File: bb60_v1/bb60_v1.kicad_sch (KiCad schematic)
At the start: 0 parts

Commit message: added microcontroller, decoupling capacitors
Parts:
- added C1, C2, C3, C4, C5: 100nF, symbol Device:C_Small
- added C6: 10uF, symbol Device:C_Small
- added U1: STM32F072CBTx, Package_QFP:LQFP-48_7x7mm_P0.5mm, symbol MCU_ST_STM32F0:STM32F072CBTx
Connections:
- new net +3.3V: C1.1, C2.1, C3.1, C4.1, C5.1, C6.1, U1.1 (VBAT), U1.24 (VDD), U1.36 (VDDIO2), U1.48 (VDD), U1.9 (VDDA)
- new net GND: C1.2, C2.2, C3.2, C4.2, C5.2, C6.2, U1.23 (VSS), U1.35 (VSS), U1.47 (VSS), U1.8 (VSSA)

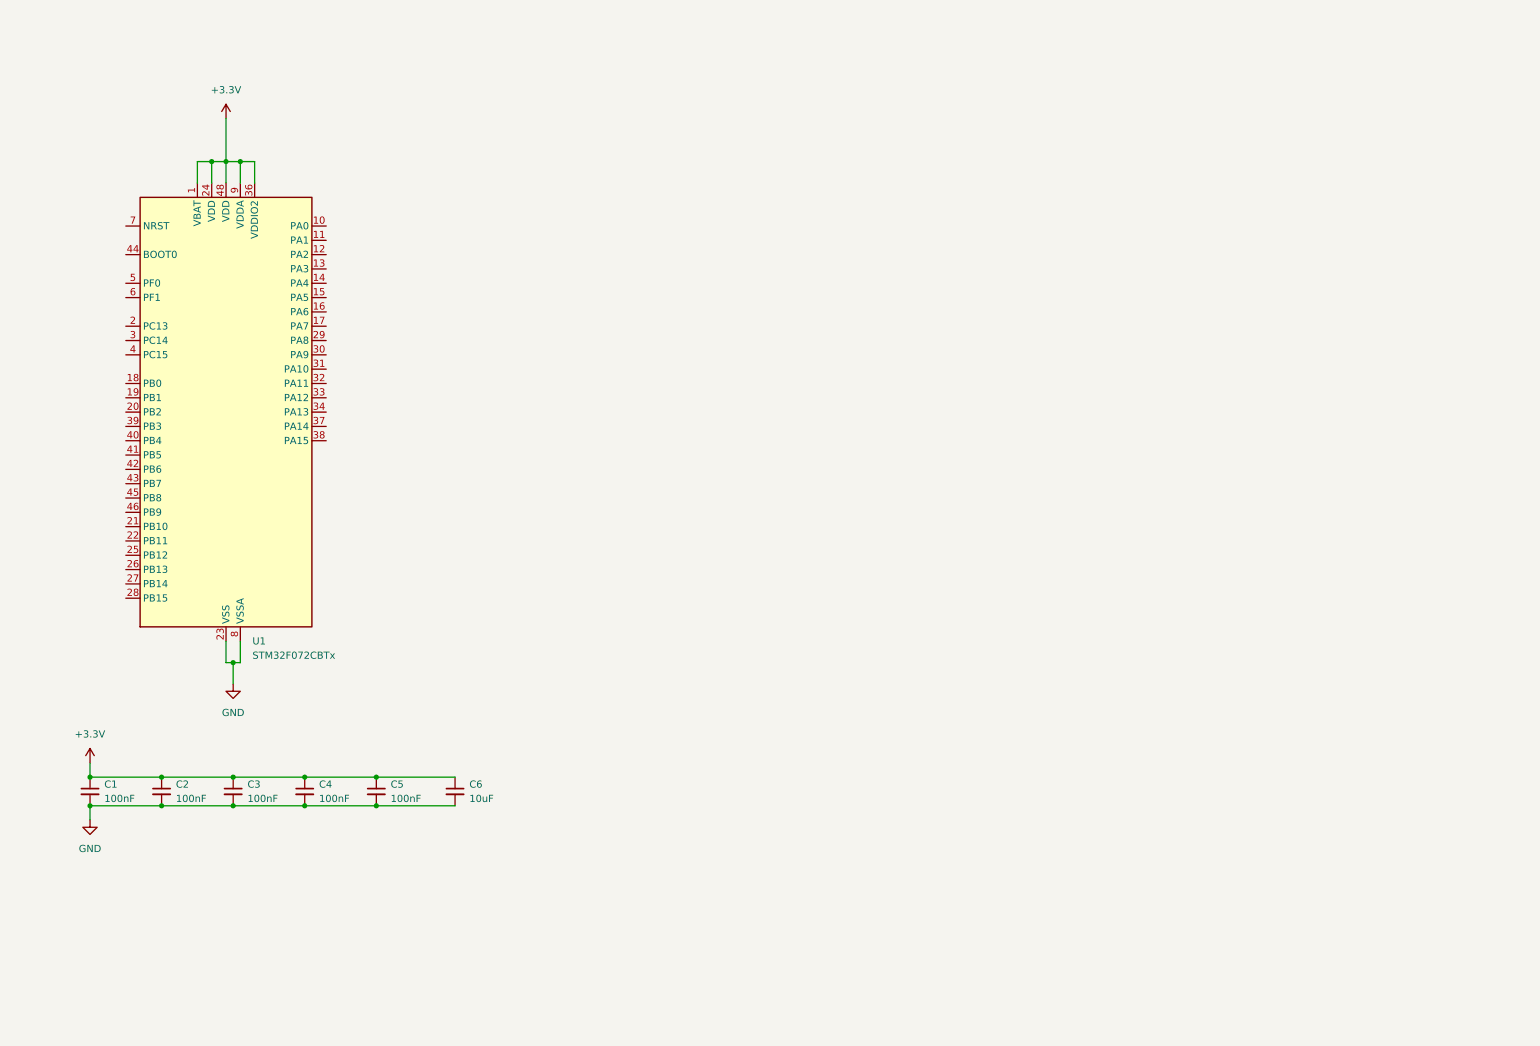
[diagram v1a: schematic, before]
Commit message: added voltage regulator, jst connector, matrix
voltage regular and matrix are unfinished
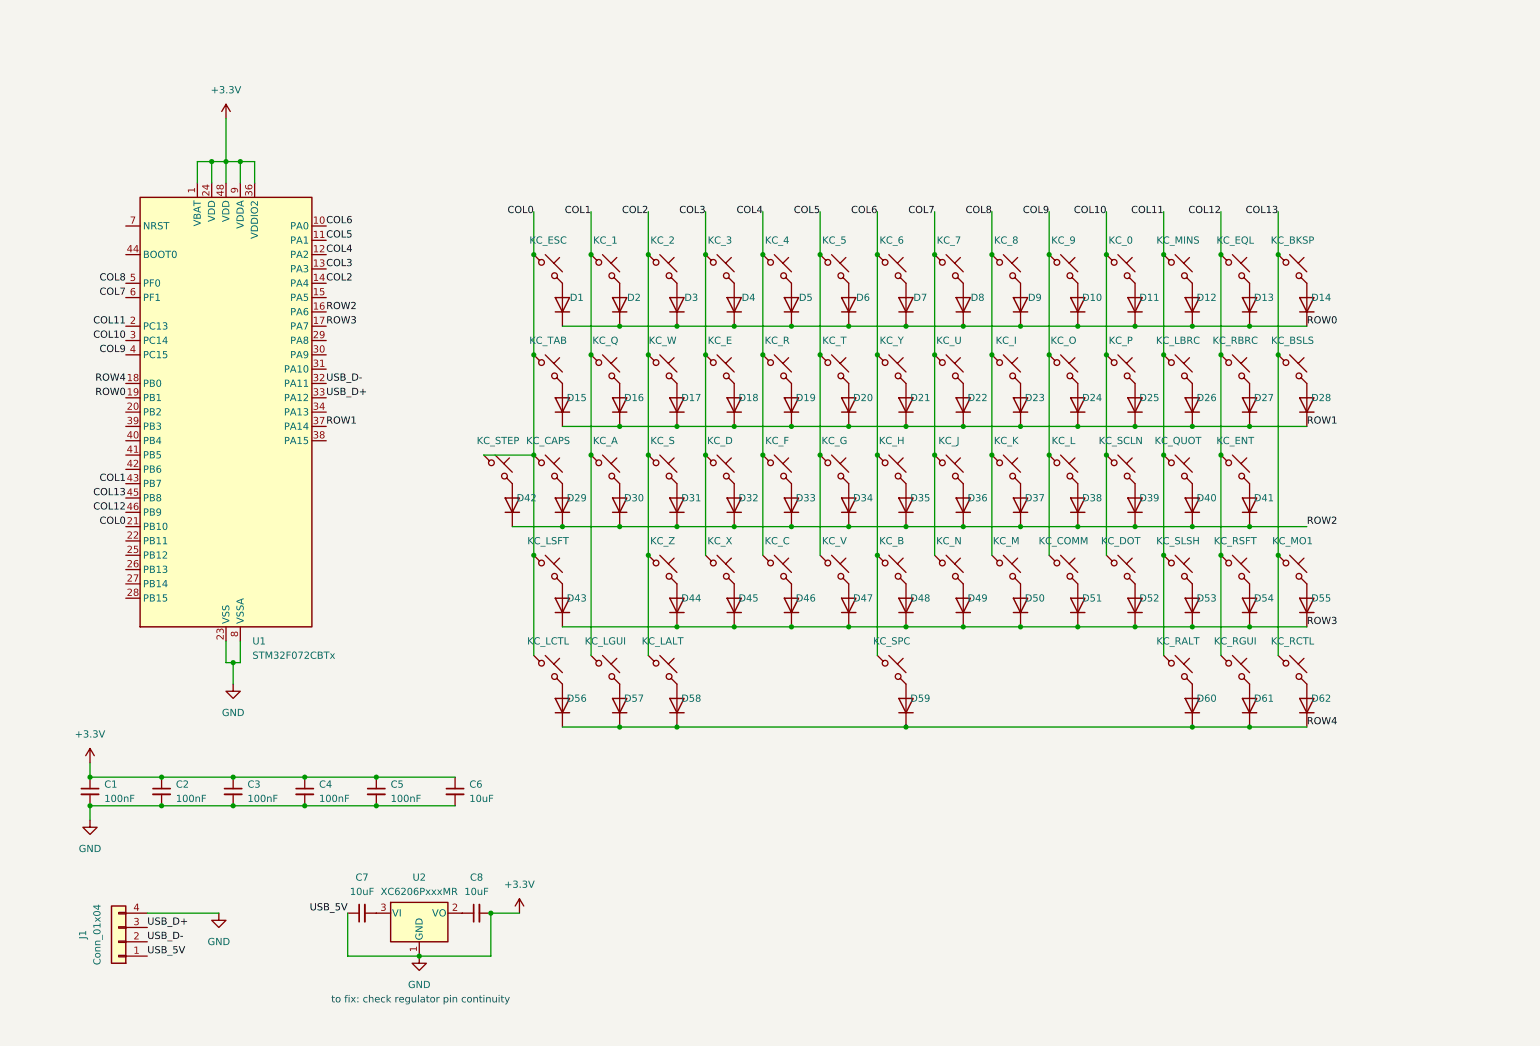
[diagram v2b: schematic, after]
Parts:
- added C7, C8: 10uF, symbol Device:C_Small
- added D1, D10, D11, D12, D13, D14, D15, D16, D17, D18, D19, D2, D20, D21, D22, D23, D24, D25, D26, D27, D28, D29, D3, D30, D31, D32, D33, D34, D35, D36, D37, D38, D39, D4, D40, D41, D42, D43, D44, D45, D46, D47, D48, D49, D5, D50, D51, D52, D53, D54, D55, D56, D57, D58, D59, D6, D60, D61, D62, D7, D8, D9: 1N4148, Diode_THT:D_DO-35_SOD27_P7.62mm_Horizontal, symbol Diode:1N4148
- added J1: Conn_01x04, Connector_JST:JST_SH_SM04B-SRSS-TB_1x04-1MP_P1.00mm_Horizontal, symbol Connector_Generic:Conn_01x04
- added KC_0, KC_1, KC_2, KC_3, KC_4, KC_5, KC_6, KC_7, KC_8, KC_9, KC_A, KC_B, KC_BKSP, KC_BSLS, KC_C, KC_CAPS, KC_COMM, KC_D, KC_DOT, KC_E, KC_ENT, KC_EQL, KC_ESC, KC_F, KC_G, KC_H, KC_I, KC_J, KC_K, KC_L, KC_LALT, KC_LBRC, KC_LCTL, KC_LGUI, KC_LSFT, KC_M, KC_MINS, KC_MO1, KC_N, KC_O, KC_P, KC_Q, KC_QUOT, KC_R, KC_RALT, KC_RBRC, KC_RCTL, KC_RGUI, KC_RSFT, KC_S, KC_SCLN, KC_SLSH, KC_SPC, KC_STEP, KC_T, KC_TAB, KC_U, KC_V, KC_W, KC_X, KC_Y, KC_Z: MX_SW_solder, marbastlib-mx:SW_MX_1u, symbol marbastlib-mx:MX_SW_solder
- added U2: XC6206PxxxMR, Package_TO_SOT_SMD:SOT-23-3, symbol Regulator_Linear:XC6206PxxxMR
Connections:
- net GND is gone; now on net +3.3V: C1.2, C2.2, C3.2, C4.2, C5.2, C6.2, U1.23 (VSS), U1.35 (VSS), U1.47 (VSS), U1.8 (VSSA)
- net +3.3V: now also C7.1, C8.2, J1.1 (Pin_1), J1.4 (Pin_4), U2.1 (GND)
- net COL6: now reaches U1.10 (PA0)
- net COL6: now also KC_6.1, KC_B.1, KC_H.1, KC_SPC.1, KC_Y.1
- net COL5: now reaches U1.11 (PA1)
- net COL5: now also KC_5.1, KC_G.1, KC_T.1, KC_V.1
- net COL4: now reaches U1.12 (PA2)
- net COL4: now also KC_4.1, KC_C.1, KC_F.1, KC_R.1
- net COL3: now reaches U1.13 (PA3)
- net COL3: now also KC_3.1, KC_D.1, KC_E.1, KC_X.1
- net COL2: now reaches U1.14 (PA4)
- net COL2: now also KC_2.1, KC_LALT.1, KC_S.1, KC_W.1, KC_Z.1
- net ROW2: now reaches U1.16 (PA6)
- net ROW2: now also D29.1 (K), D30.1 (K), D31.1 (K), D32.1 (K), D33.1 (K), D34.1 (K), D35.1 (K), D36.1 (K), D37.1 (K), D38.1 (K), D39.1 (K), D40.1 (K), D41.1 (K), D42.1 (K)
- net ROW3: now reaches U1.17 (PA7)
- net ROW3: now also D43.1 (K), D44.1 (K), D45.1 (K), D46.1 (K), D47.1 (K), D48.1 (K), D49.1 (K), D50.1 (K), D51.1 (K), D52.1 (K), D53.1 (K), D54.1 (K), D55.1 (K)
- net ROW4: now reaches U1.18 (PB0)
- net ROW4: now also D56.1 (K), D57.1 (K), D58.1 (K), D59.1 (K), D60.1 (K), D61.1 (K), D62.1 (K)
- net ROW0: now reaches U1.19 (PB1)
- net ROW0: now also D1.1 (K), D10.1 (K), D11.1 (K), D12.1 (K), D13.1 (K), D14.1 (K), D2.1 (K), D3.1 (K), D4.1 (K), D5.1 (K), D6.1 (K), D7.1 (K), D8.1 (K), D9.1 (K)
- net COL11: now reaches U1.2 (PC13)
- net COL11: now also KC_LBRC.1, KC_MINS.1, KC_QUOT.1, KC_RALT.1, KC_SLSH.1
- net COL0: now reaches U1.21 (PB10)
- net COL0: now also KC_CAPS.1, KC_ESC.1, KC_LCTL.1, KC_LSFT.1, KC_STEP.1, KC_TAB.1
- net COL10: now reaches U1.3 (PC14)
- net COL10: now also KC_0.1, KC_DOT.1, KC_P.1, KC_SCLN.1
- net USB_D-: now reaches U1.32 (PA11)
- net USB_D-: now also J1.2 (Pin_2)
- net USB_D+: now reaches U1.33 (PA12)
- net USB_D+: now also J1.3 (Pin_3)
- net ROW1: now reaches U1.37 (PA14)
- net ROW1: now also D15.1 (K), D16.1 (K), D17.1 (K), D18.1 (K), D19.1 (K), D20.1 (K), D21.1 (K), D22.1 (K), D23.1 (K), D24.1 (K), D25.1 (K), D26.1 (K), D27.1 (K), D28.1 (K)
- net COL9: now reaches U1.4 (PC15)
- net COL9: now also KC_9.1, KC_COMM.1, KC_L.1, KC_O.1
- net COL1: now reaches U1.43 (PB7)
- net COL1: now also KC_1.1, KC_A.1, KC_LGUI.1, KC_Q.1
- net COL13: now reaches U1.45 (PB8)
- net COL13: now also KC_BKSP.1, KC_BSLS.1, KC_MO1.1, KC_RCTL.1
- net COL12: now reaches U1.46 (PB9)
- net COL12: now also KC_ENT.1, KC_EQL.1, KC_RBRC.1, KC_RGUI.1, KC_RSFT.1
- net COL8: now reaches U1.5 (PF0)
- net COL8: now also KC_8.1, KC_I.1, KC_K.1, KC_M.1
- net COL7: now reaches U1.6 (PF1)
- net COL7: now also KC_7.1, KC_J.1, KC_N.1, KC_U.1
- new net: D34.2 (A), KC_G.2
- new net: D20.2 (A), KC_T.2
- new net: D25.2 (A), KC_P.2
- new net: D45.2 (A), KC_X.2
- new net: D36.2 (A), KC_J.2
- new net: D38.2 (A), KC_L.2
- new net: D61.2 (A), KC_RGUI.2
- new net: D60.2 (A), KC_RALT.2
- new net: D2.2 (A), KC_1.2
- new net: D5.2 (A), KC_4.2
- new net: D11.2 (A), KC_0.2
- new net: D27.2 (A), KC_RBRC.2
- new net: D52.2 (A), KC_DOT.2
- new net: D29.2 (A), KC_CAPS.2
- new net: C7.2, U2.3 (VI)
- new net: D28.2 (A), KC_BSLS.2
- new net: D40.2 (A), KC_QUOT.2
- new net: D58.2 (A), KC_LALT.2
- new net: D17.2 (A), KC_W.2
- new net: D6.2 (A), KC_5.2
- new net: D14.2 (A), KC_BKSP.2
- new net: D3.2 (A), KC_2.2
- new net: D59.2 (A), KC_SPC.2
- new net: D32.2 (A), KC_D.2
- new net: D39.2 (A), KC_SCLN.2
- new net: D33.2 (A), KC_F.2
- new net: D35.2 (A), KC_H.2
- new net: D37.2 (A), KC_K.2
- new net: D47.2 (A), KC_V.2
- new net: D22.2 (A), KC_U.2
- new net: D7.2 (A), KC_6.2
- new net: D1.2 (A), KC_ESC.2
- new net: D54.2 (A), KC_RSFT.2
- new net: D44.2 (A), KC_Z.2
- new net: D48.2 (A), KC_B.2
- new net: D18.2 (A), KC_E.2
- new net: D10.2 (A), KC_9.2
- new net: D12.2 (A), KC_MINS.2
- new net: D62.2 (A), KC_RCTL.2
- new net: D21.2 (A), KC_Y.2
- new net: D24.2 (A), KC_O.2
- new net: D56.2 (A), KC_LCTL.2
- new net: D53.2 (A), KC_SLSH.2
- new net: C8.1, U2.2 (VO)
- new net: D8.2 (A), KC_7.2
- new net: D31.2 (A), KC_S.2
- new net: D46.2 (A), KC_C.2
- new net: D50.2 (A), KC_M.2
- new net: D41.2 (A), KC_ENT.2
- new net: D51.2 (A), KC_COMM.2
- new net: D49.2 (A), KC_N.2
- new net: D30.2 (A), KC_A.2
- new net: D16.2 (A), KC_Q.2
- new net: D57.2 (A), KC_LGUI.2
- new net: D19.2 (A), KC_R.2
- new net: D9.2 (A), KC_8.2
- new net: D15.2 (A), KC_TAB.2
- new net: D13.2 (A), KC_EQL.2
- new net: D4.2 (A), KC_3.2
- new net: D42.2 (A), KC_STEP.2
- new net: D43.2 (A), KC_LSFT.2
- new net: D26.2 (A), KC_LBRC.2
- new net: D55.2 (A), KC_MO1.2
- new net: D23.2 (A), KC_I.2
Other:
- note added: "to fix: check regulator pin continuity"

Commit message: Visual changes to schematic
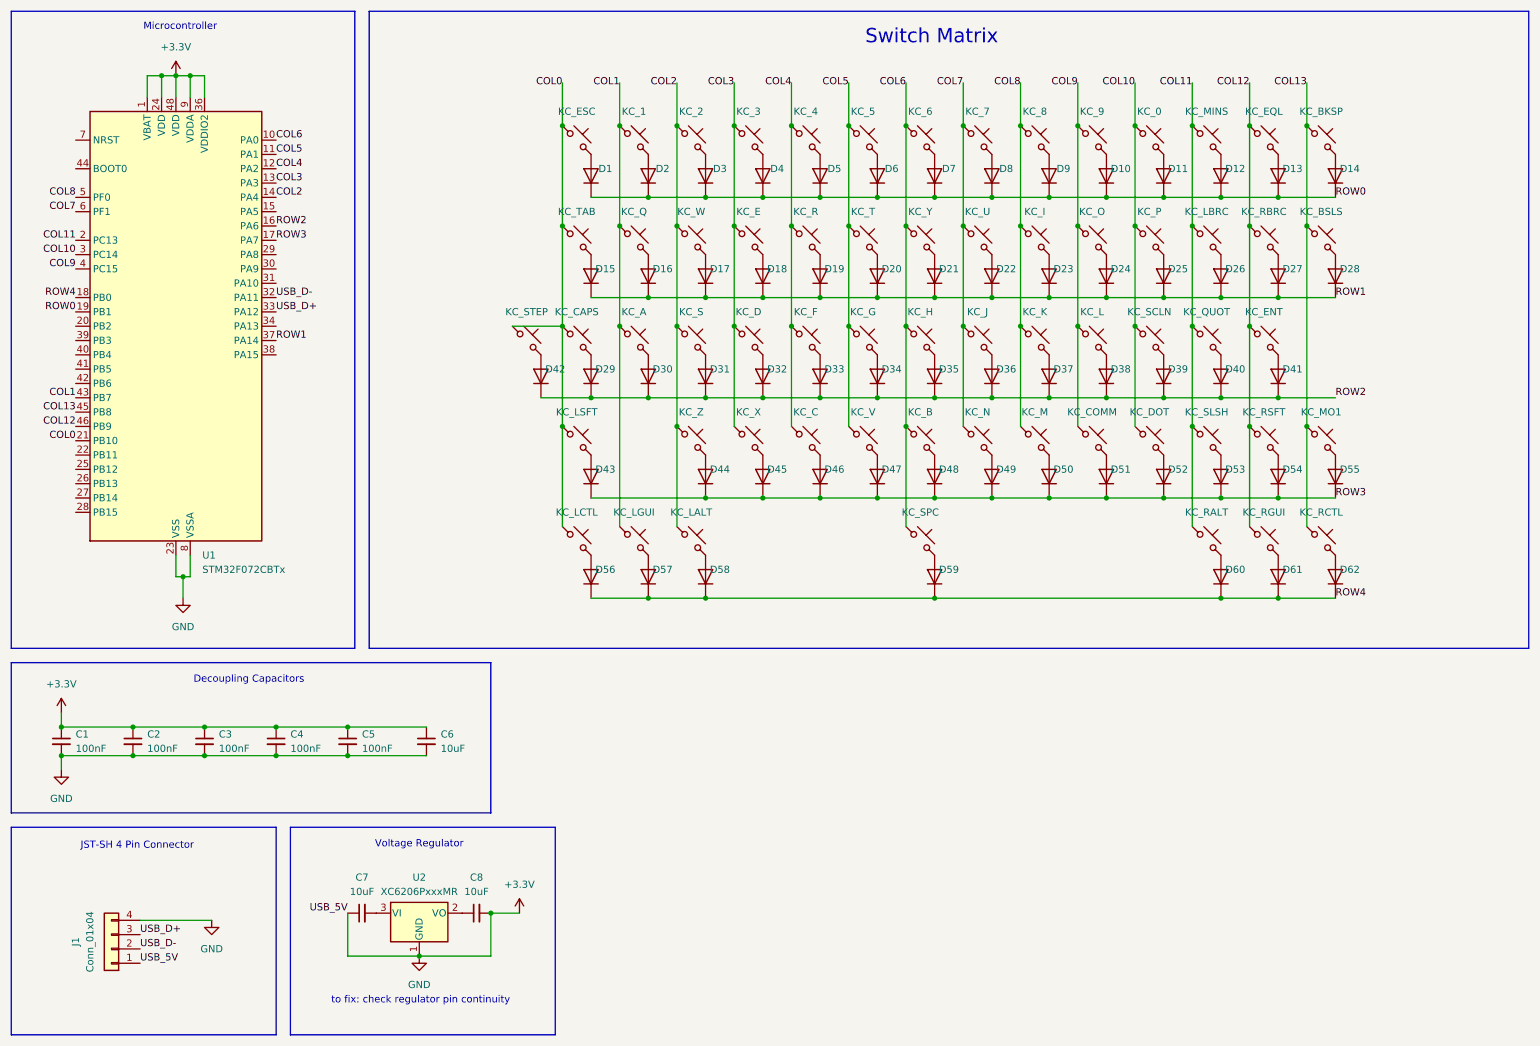
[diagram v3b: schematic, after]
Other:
- note added: "Decoupling Capacitors"
- note added: "JST-SH 4 Pin Connector"
- note added: "Microcontroller"
- note added: "Switch Matrix"
- note added: "Voltage Regulator"
- moved on the sheet: C1, C2, C3, C4, C5, C6, D1, D10, D11, D12, D13, D14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

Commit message: Added USB Resistors, ESD Protection, Reset and bootloader buttons
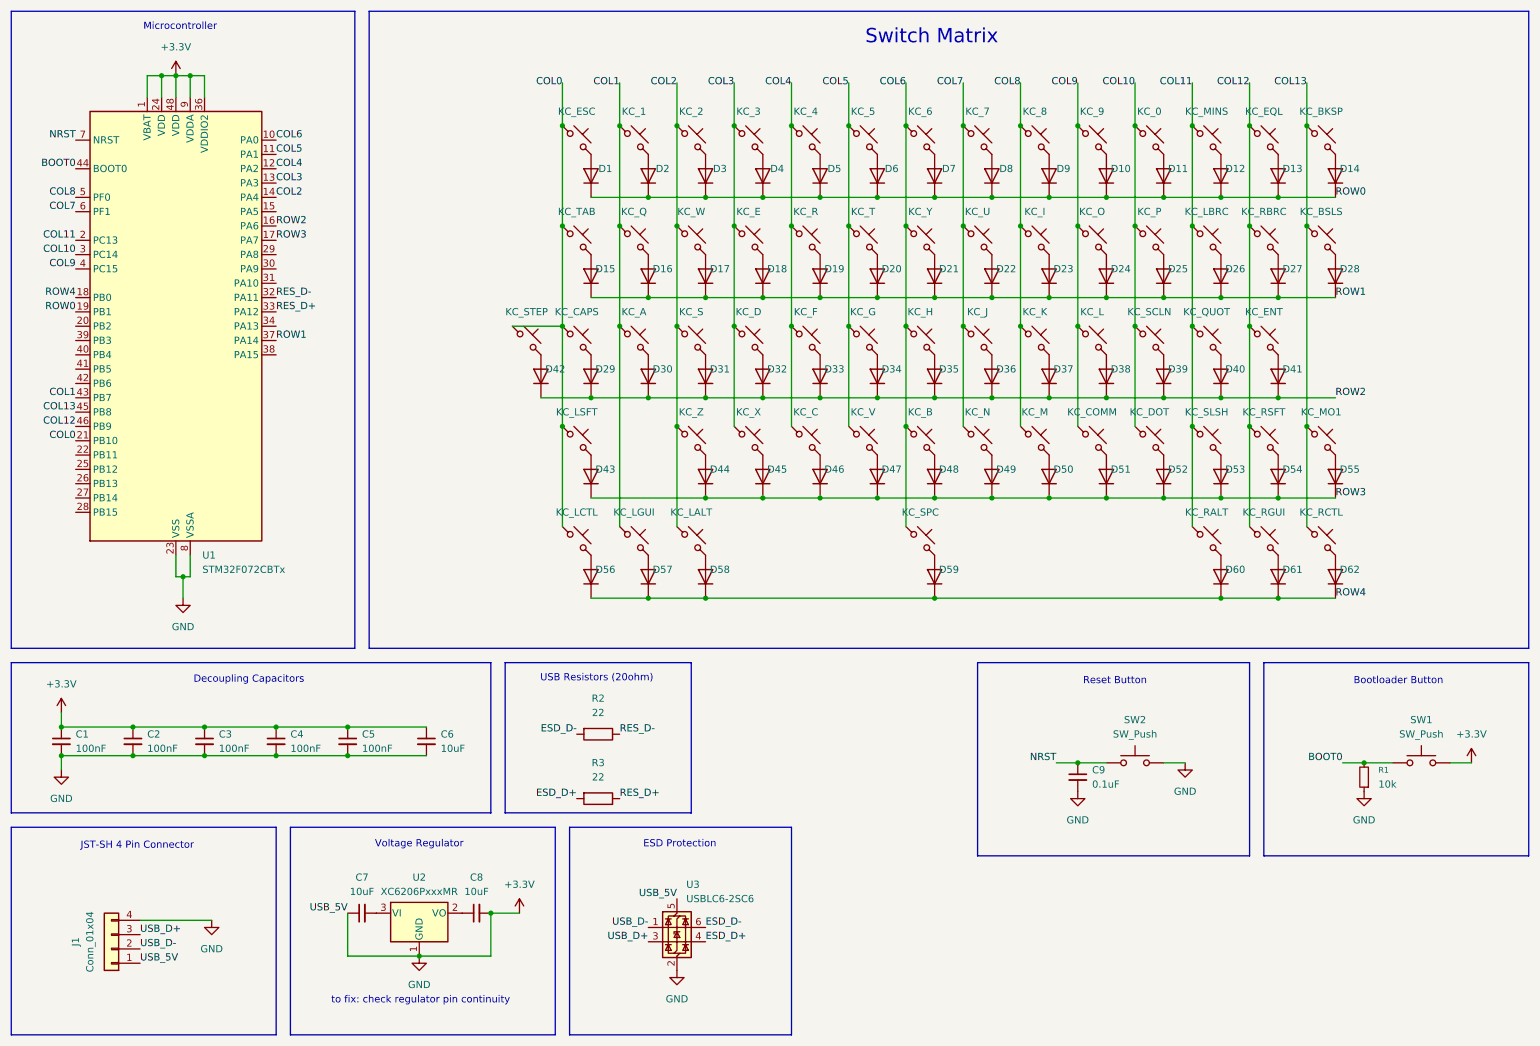
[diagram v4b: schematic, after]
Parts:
- added C9: 0.1uF, symbol Device:C_Small
- added R1: 10k, symbol Device:R_Small
- added R2, R3: 22, symbol Device:R
- added SW1, SW2: SW_Push, symbol Switch:SW_Push
- added U3: USBLC6-2SC6, Package_TO_SOT_SMD:SOT-23-6, symbol Power_Protection:USBLC6-2SC6
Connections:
- net +3.3V: now also C9.2, R1.1, SW1.2, SW2.2, U3.2 (GND), U3.5 (VBUS)
- net USB_D+: now also U3.3 (I/O2); no longer U1.33 (PA12)
- net USB_D-: now also U3.1 (I/O1); no longer U1.32 (PA11)
- net BOOT0: now reaches U1.44 (BOOT0)
- net BOOT0: now also R1.2, SW1.1
- net NRST: now reaches U1.7 (NRST)
- net NRST: now also C9.1, SW2.1
- new net ESD_D+: R3.2, U3.4 (I/O2)
- new net ESD_D-: R2.2, U3.6 (I/O1)
- new net RES_D+: R3.1, U1.33 (PA12)
- new net RES_D-: R2.1, U1.32 (PA11)
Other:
- note added: "Bootloader Button"
- note added: "ESD Protection"
- note added: "Reset Button"
- note added: "USB Resistors (20ohm)"

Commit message: Small changes to schematic
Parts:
- added D63: 1N4148, Diode_THT:D_DO-35_SOD27_P7.62mm_Horizontal, symbol Diode:1N4148
- added KC_BKSP1: MX_SW_solder, marbastlib-mx:SW_MX_1u, symbol marbastlib-mx:MX_SW_solder
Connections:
- net +3.3V: now also U2.2 (VO); no longer C1.2, C2.2, C3.2, C4.2, C5.2, C6.2, C7.1, C9.2, J1.1 (Pin_1), J1.4 (Pin_4), R1.1, SW2.2, U1.23 (VSS), U1.35 (VSS), U1.47 (VSS), U1.8 (VSSA), U2.1 (GND), U3.2 (GND), U3.5 (VBUS)
- net COL13: now also KC_BKSP1.1
- net ROW0: now also D63.1 (K)
- net +5V: now reaches C7.2, U2.3 (VI)
- net +5V: now also J1.1 (Pin_1), U3.5 (VBUS)
- net GND: now reaches C8.1
- net GND: now also C1.2, C2.2, C3.2, C4.2, C5.2, C6.2, C7.1, C9.2, J1.4 (Pin_4), R1.1, SW2.2, U1.23 (VSS), U1.35 (VSS), U1.47 (VSS), U1.8 (VSSA), U2.1 (GND), U3.2 (GND); no longer U2.2 (VO)
- new net: D63.2 (A), KC_BKSP1.2
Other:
- moved on the sheet: C7, C8
